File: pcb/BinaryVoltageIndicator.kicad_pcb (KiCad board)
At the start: 2 copper layers, 20 x 10 mm, 17 parts, among them J1 Conn, Q1 2N7002, U1 MCP65R41-2402

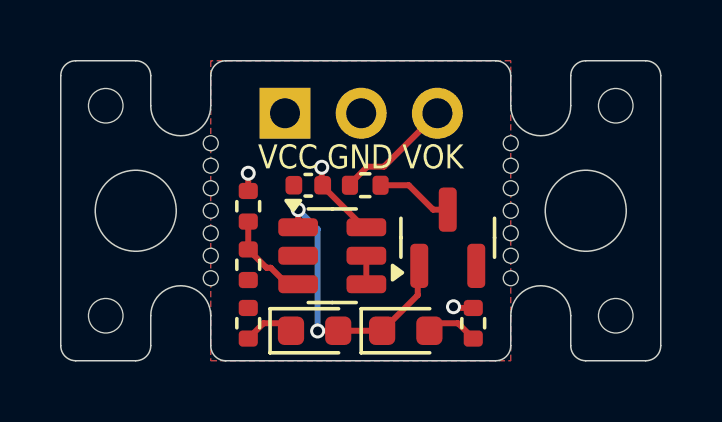
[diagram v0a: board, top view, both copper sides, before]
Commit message: fix: change measurement resistors to 0603
the 0402 resistors in JLCPCBs standard library are 5% - too much for this to work properly
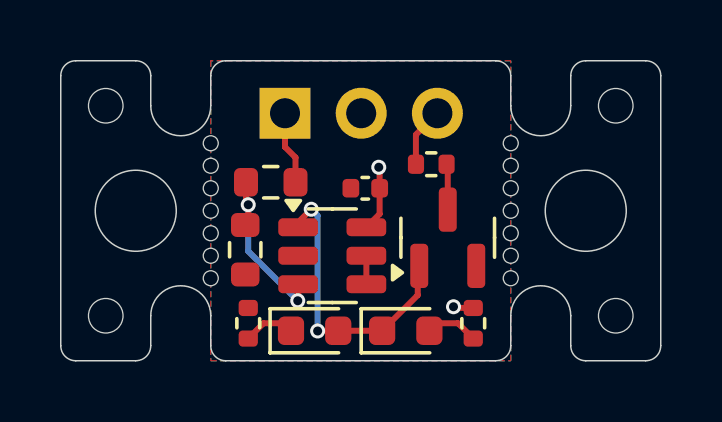
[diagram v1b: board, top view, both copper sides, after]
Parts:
- R1, R2: footprint Resistor_SMD:R_0402_1005Metric -> Resistor_SMD:R_0603_1608Metric
- moved R5 2.31 mm to (129.8, 103.5)
- moved C1 1.90 mm to (127.7, 104.2)
- moved R1 1.10 mm to (124.5, 104.0), turned to 0 degrees
- moved R2 0.51 mm to (123.7, 106.3)
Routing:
- net /Vmeas: track 3.07 -> 6.53 mm, vias 0 -> 2
- net /~{VOK}: track 4.08 -> 2.00 mm
- net VCC: track 3.93 -> 5.32 mm, vias 3 -> 2
- net Net-(Q1-D): track 2.58 -> 1.53 mm
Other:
- board text removed: "VCC GND VOK"
